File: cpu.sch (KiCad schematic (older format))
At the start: 24 parts, among them SW1 RESET, SW2 STEP, U1 Z80CPU, U2 74HC04, Y1 7.3728MHz

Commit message: New layout complete. Now with rc2014 compat. slots!
Plus on board address decoding, single stepping using M1 line so button
is click per instruction. Board is also much smaller!
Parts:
- removed C6: 1uF, Capacitors_ThroughHole:C_Radial_D5_L11_P2.5, symbol CP
- removed D2, D3: LED, LEDs:LED-3MM, symbol LED
- removed D8: D, Diodes_ThroughHole:Diode_DO-41_SOD81_Horizontal_RM10, symbol D
- removed JP1: JUMPER3, Pin_Headers:Pin_Header_Straight_1x03, symbol JUMPER3
- removed R11: 1K, Resistors_ThroughHole:Resistor_Horizontal_RM7mm, symbol R
- removed R12, R14: 220, Resistors_ThroughHole:Resistor_Horizontal_RM7mm, symbol R
- removed R13: 82K, Resistors_ThroughHole:Resistor_Horizontal_RM7mm, symbol R
- removed R15: 18K, Resistors_ThroughHole:Resistor_Horizontal_RM7mm, symbol R
- added C10, C6, C8, C9: 10n, Capacitors_ThroughHole:C_Disc_D3_P2.5, symbol C
- added JP1: JUMPER, Pin_Headers:Pin_Header_Straight_1x02, symbol JUMPER
- added R2: 1M, Resistors_ThroughHole:Resistor_Horizontal_RM7mm, symbol R
- added R3, R7: 1K, Resistors_ThroughHole:Resistor_Horizontal_RM7mm, symbol R
- added R6: 10K, Resistors_ThroughHole:Resistor_Horizontal_RM7mm, symbol R
- added U4, U6: LM555N, Housings_DIP:DIP-8_W7.62mm_LongPads, symbol LM555N
- added U5: 74HC74, Housings_DIP:DIP-14_W7.62mm_LongPads, symbol 74HC74
- C1, C12: value 100nF -> 100n
- R5: value 1M -> 1K
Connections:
- wire segments 140 -> 155
- no-connect marks 1 -> 8
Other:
- moved on the sheet: C1, C12, C2, C3, R1, RR1, SW1, U1

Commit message: Another new board layout. Few tidy ups.
Removed the single step circuit, not worth the board space and headache.
Added legend for the IO slot for easy reference. Still toying where to
put the power LED, annoying me with that resistor. Think I'm happy with
it now. Spaced things out a little to make it easy for manufacture, made
sure no traces are near board edges as much as possible.
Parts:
- removed C10, C6, C8, C9: 10n, Capacitors_ThroughHole:C_Disc_D3_P2.5, symbol C
- removed JP1: JUMPER, Pin_Headers:Pin_Header_Straight_1x02, symbol JUMPER
- removed R5, R7: 1K, Resistors_ThroughHole:Resistor_Horizontal_RM7mm, symbol R
- removed R6: 10K, Resistors_ThroughHole:Resistor_Horizontal_RM7mm, symbol R
- removed SW2: STEP, Buttons_Switches_ThroughHole:SW_PUSH_SMALL, symbol SW_PUSH
- removed unit 4 of U2
- removed unit 6 of U2
- removed U4, U6: LM555N, Housings_DIP:DIP-8_W7.62mm_LongPads, symbol LM555N
- removed U5: 74HC74, Housings_DIP:DIP-14_W7.62mm_LongPads, symbol 74HC74
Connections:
- wire segments 155 -> 116
- no-connect marks 8 -> 4

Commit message: * Replaced one card slot with an updated expansion connector. * Replaced '138 with GAL. * Implemented interrupt priority lines IEI/IEO. * Replaced discrete oscillator with 14/8 pin DIP oscillator block.
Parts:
- removed C4, C5: 22pF, Capacitors_ThroughHole:C_Disc_D3_P2.5, symbol C
- removed R2: 1M, Resistors_ThroughHole:Resistor_Horizontal_RM7mm, symbol R
- removed R3: 1K, Resistors_ThroughHole:Resistor_Horizontal_RM7mm, symbol R
- removed U2: 74HC04, Housings_DIP:DIP-14_W7.62mm_LongPads, symbol 74HC04
- removed Y1: 7.3728MHz, Crystals:Crystal_HC49-U_Vertical, symbol Crystal
- added U?: DIP_OSCILLATOR, symbol DIP_OSCILLATOR
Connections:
- wire segments 116 -> 104
- no-connect marks 4 -> 2
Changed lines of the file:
@@
 LIBS:6850
 LIBS:nrc2016
+LIBS:atf16v8cv
+LIBS:62256
 LIBS:z80-cache
 EELAYER 25 0
@@
 D7
 $Comp
-L VCC #PWR010
+L VCC #PWR16
 U 1 1 577A54FB
 P 8250 950
-F 0 "#PWR010" H 8250 800 50  0001 C CNN
+F 0 "#PWR16" H 8250 800 50  0001 C CNN
 F 1 "VCC" H 8250 1100 50  0000 C CNN
 F 2 "" H 8250 950 50  0000 C CNN
@@
 $EndComp
 $Comp
-L GND #PWR011
+L GND #PWR17
 U 1 1 577A554F
 P 8250 4250
-F 0 "#PWR011" H 8250 4000 50  0001 C CNN
+F 0 "#PWR17" H 8250 4000 50  0001 C CNN
 F 1 "GND" H 8250 4100 50  0000 C CNN
 F 2 "" H 8250 4250 50  0000 C CNN
@@
 $EndComp
 $Comp
-L GND #PWR012
+L GND #PWR11
 U 1 1 577B455D
 P 3050 1450
-F 0 "#PWR012" H 3050 1200 50  0001 C CNN
+F 0 "#PWR11" H 3050 1200 50  0001 C CNN
 F 1 "GND" H 3050 1300 50  0000 C CNN
 F 2 "" H 3050 1450 50  0000 C CNN
@@
 $EndComp
 $Comp
-L GND #PWR013
+L GND #PWR12
 U 1 1 577B48FE
 P 4050 1450
-F 0 "#PWR013" H 4050 1200 50  0001 C CNN
+F 0 "#PWR12" H 4050 1200 50  0001 C CNN
 F 1 "GND" H 4050 1300 50  0000 C CNN
 F 2 "" H 4050 1450 50  0000 C CNN
@@
 $EndComp
 $Comp
-L VCC #PWR014
+L VCC #PWR14
 U 1 1 577B4D04
 P 4650 650
-F 0 "#PWR014" H 4650 500 50  0001 C CNN
+F 0 "#PWR14" H 4650 500 50  0001 C CNN
 F 1 "VCC" H 4650 800 50  0000 C CNN
 F 2 "" H 4650 650 50  0000 C CNN
@@
 $EndComp
 $Comp
-L GND #PWR015
+L GND #PWR19
 U 1 1 577B59DE
 P 9750 6050
-F 0 "#PWR015" H 9750 5800 50  0001 C CNN
+F 0 "#PWR19" H 9750 5800 50  0001 C CNN
 F 1 "GND" H 9750 5900 50  0000 C CNN
 F 2 "" H 9750 6050 50  0000 C CNN
@@
 $EndComp
 $Comp
-L GND #PWR016
+L GND #PWR21
 U 1 1 577B5A43
 P 10150 6050
-F 0 "#PWR016" H 10150 5800 50  0001 C CNN
+F 0 "#PWR21" H 10150 5800 50  0001 C CNN
 F 1 "GND" H 10150 5900 50  0000 C CNN
 F 2 "" H 10150 6050 50  0000 C CNN
@@
 $EndComp
 $Comp
-L VCC #PWR017
+L VCC #PWR22
 U 1 1 5794221C
 P 10550 5600
-F 0 "#PWR017" H 10550 5450 50  0001 C CNN
+F 0 "#PWR22" H 10550 5450 50  0001 C CNN
 F 1 "VCC" H 10550 5750 50  0000 C CNN
 F 2 "" H 10550 5600 50  0000 C CNN
@@
 $EndComp
 $Comp
-L GND #PWR018
+L GND #PWR23
 U 1 1 57942290
 P 10550 6100
-F 0 "#PWR018" H 10550 5850 50  0001 C CNN
+F 0 "#PWR23" H 10550 5850 50  0001 C CNN
 F 1 "GND" H 10550 5950 50  0000 C CNN
 F 2 "" H 10550 6100 50  0000 C CNN
@@
 $EndComp
 $Comp
-L VCC #PWR019
+L VCC #PWR15
 U 1 1 57945470
 P 6100 1550
-F 0 "#PWR019" H 6100 1400 50  0001 C CNN
+F 0 "#PWR15" H 6100 1400 50  0001 C CNN
 F 1 "VCC" H 6100 1700 50  0000 C CNN
 F 2 "" H 6100 1550 50  0000 C CNN
@@
 	1    0    0    -1
 $EndComp
-$Comp
-L R R2
-U 1 1 57991B52
-P 1350 1650
-F 0 "R2" V 1430 1650 50  0000 C CNN
-F 1 "1M" V 1350 1650 50  0000 C CNN
-F 2 "Resistors_ThroughHole:Resistor_Horizontal_RM7mm" V 1280 1650 50  0001 C CNN
-F 3 "" H 1350 1650 50  0000 C CNN
-	1    1350 1650
-	0    1    1    0
-$EndComp
-$Comp
-L R R3
-U 1 1 57991D5E
-P 1850 2300
-F 0 "R3" V 1930 2300 50  0000 C CNN
-F 1 "1K" V 1850 2300 50  0000 C CNN
-F 2 "Resistors_ThroughHole:Resistor_Horizontal_RM7mm" V 1780 2300 50  0001 C CNN
-F 3 "" H 1850 2300 50  0000 C CNN
-	1    1850 2300
-	1    0    0    -1
-$EndComp
-$Comp
-L Crystal Y1
-U 1 1 57991DBB
-P 1350 2550
-F 0 "Y1" H 1350 2700 50  0000 C CNN
-F 1 "7.3728MHz" H 1350 2400 50  0000 C CNN
-F 2 "Crystals:Crystal_HC49-U_Vertical" H 1350 2550 50  0001 C CNN
-F 3 "" H 1350 2550 50  0000 C CNN
-	1    1350 2550
-	1    0    0    -1
-$EndComp
-$Comp
-L C C4
-U 1 1 579921C3
-P 850 2800
-F 0 "C4" H 875 2900 50  0000 L CNN
-F 1 "22pF" H 875 2700 50  0000 L CNN
-F 2 "Capacitors_ThroughHole:C_Disc_D3_P2.5" H 888 2650 50  0001 C CNN
-F 3 "" H 850 2800 50  0000 C CNN
-	1    850  2800
-	1    0    0    -1
-$EndComp
-$Comp
-L C C5
-U 1 1 57992226
-P 1850 2800
-F 0 "C5" H 1875 2900 50  0000 L CNN
-F 1 "22pF" H 1875 2700 50  0000 L CNN
-F 2 "Capacitors_ThroughHole:C_Disc_D3_P2.5" H 1888 2650 50  0001 C CNN
-F 3 "" H 1850 2800 50  0000 C CNN
-	1    1850 2800
-	1    0    0    -1
-$EndComp
-$Comp
-L GND #PWR020
-U 1 1 579925A6
-P 850 3050
-F 0 "#PWR020" H 850 2800 50  0001 C CNN
-F 1 "GND" H 850 2900 50  0000 C CNN
-F 2 "" H 850 3050 50  0000 C CNN
-F 3 "" H 850 3050 50  0000 C CNN
-	1    850  3050
-	1    0    0    -1
-$EndComp
-$Comp
-L GND #PWR021
-U 1 1 579925F6
-P 1850 3050
-F 0 "#PWR021" H 1850 2800 50  0001 C CNN
-F 1 "GND" H 1850 2900 50  0000 C CNN
-F 2 "" H 1850 3050 50  0000 C CNN
-F 3 "" H 1850 3050 50  0000 C CNN
-	1    1850 3050
-	1    0    0    -1
-$EndComp
 Text Label 7250 2200 0    60   ~ 0
 ~M1
@@
 ~WAIT
 $Comp
-L 74HC04 U2
-U 1 1 57997E58
-P 1350 2050
-F 0 "U2" H 1500 2150 50  0000 C CNN
-F 1 "74HC04" H 1550 1950 50  0000 C CNN
-F 2 "Housings_DIP:DIP-14_W7.62mm_LongPads" H 1350 2050 50  0001 C CNN
-F 3 "" H 1350 2050 50  0000 C CNN
-	1    1350 2050
-	1    0    0    -1
-$EndComp
-$Comp
-L 74HC04 U2
-U 2 1 579987FC
-P 2350 2050
-F 0 "U2" H 2500 2150 50  0000 C CNN
-F 1 "74HC04" H 2550 1950 50  0000 C CNN
-F 2 "Housings_DIP:DIP-14_W7.62mm_LongPads" H 2350 2050 50  0001 C CNN
-F 3 "" H 2350 2050 50  0000 C CNN
-	2    2350 2050
-	1    0    0    -1
-$EndComp
-$Comp
-L VCC #PWR022
+L VCC #PWR20
 U 1 1 579C0903
 P 10150 5600
-F 0 "#PWR022" H 10150 5450 50  0001 C CNN
+F 0 "#PWR20" H 10150 5450 50  0001 C CNN
 F 1 "VCC" H 10150 5750 50  0000 C CNN
 F 2 "" H 10150 5600 50  0000 C CNN
@@
 $EndComp
 $Comp
-L VCC #PWR023
+L VCC #PWR18
 U 1 1 579C0968
 P 9750 5600
-F 0 "#PWR023" H 9750 5450 50  0001 C CNN
+F 0 "#PWR18" H 9750 5450 50  0001 C CNN
 F 1 "VCC" H 9750 5750 50  0000 C CNN
 F 2 "" H 9750 5600 50  0000 C CNN
@@
 Connection ~ 7200 3400
 Wire Wire Line
-	1850 1650 1850 2150
-Wire Wire Line
-	850  1650 850  2650
-Wire Wire Line
-	1200 1650 850  1650
-Wire Wire Line
-	1500 1650 1850 1650
-Wire Wire Line
-	1500 2550 1850 2550
-Wire Wire Line
-	1850 2450 1850 2650
-Wire Wire Line
-	850  2550 1200 2550
-Connection ~ 1850 2550
-Connection ~ 850  2550
-Wire Wire Line
-	850  2950 850  3050
-Wire Wire Line
-	1850 2950 1850 3050
-Wire Wire Line
 	4050 700  4200 700
 Wire Wire Line
@@
 Connection ~ 5800 1750
 Wire Wire Line
-	900  2050 850  2050
-Connection ~ 850  2050
-Wire Wire Line
-	1800 2050 1900 2050
-Connection ~ 1850 2050
-Wire Wire Line
 	7100 1750 7100 3100
 Connection ~ 7100 3100
@@
 Connection ~ 7000 2000
 $Comp
-L 74HC04 U2
-U 3 1 579DE204
-P 4750 2950
-F 0 "U2" H 4900 3050 50  0000 C CNN
-F 1 "74HC04" H 4950 2850 50  0000 C CNN
-F 2 "Housings_DIP:DIP-14_W7.62mm_LongPads" H 4750 2950 50  0001 C CNN
-F 3 "" H 4750 2950 50  0000 C CNN
-	3    4750 2950
-	1    0    0    -1
-$EndComp
-$Comp
-L 74HC04 U2
-U 5 1 579DE2CC
-P 4750 3350
-F 0 "U2" H 4900 3450 50  0000 C CNN
-F 1 "74HC04" H 4950 3250 50  0000 C CNN
-F 2 "Housings_DIP:DIP-14_W7.62mm_LongPads" H 4750 3350 50  0001 C CNN
-F 3 "" H 4750 3350 50  0000 C CNN
-	5    4750 3350
-	1    0    0    -1
-$EndComp
-Wire Wire Line
-	4300 2950 4200 2950
-Wire Wire Line
-	4200 2750 4200 3350
-Wire Wire Line
-	4200 3350 4300 3350
-Connection ~ 4200 2950
-$Comp
-L VCC #PWR024
+L VCC #PWR13
 U 1 1 579DE54D
-P 4200 2750
-F 0 "#PWR024" H 4200 2600 50  0001 C CNN
-F 1 "VCC" H 4200 2900 50  0000 C CNN
-F 2 "" H 4200 2750 50  0000 C CNN
-F 3 "" H 4200 2750 50  0000 C CNN
-	1    4200 2750
-	1    0    0    -1
-$EndComp
-NoConn ~ 5200 2950
-NoConn ~ 5200 3350
+P 2500 1450
+F 0 "#PWR13" H 2500 1300 50  0001 C CNN
+F 1 "VCC" H 2500 1600 50  0000 C CNN
+F 2 "" H 2500 1450 50  0000 C CNN
+F 3 "" H 2500 1450 50  0000 C CNN
+	1    2500 1450
+	1    0    0    -1
+$EndComp
 NoConn ~ 6100 2500
+$Comp
+L DIP_OSCILLATOR U?
+U 1 1 57C09843
+P 2300 2350
+F 0 "U?" H 2650 2300 60  0000 C CNN
+F 1 "DIP_OSCILLATOR" V 2250 2650 60  0000 C CNN
+F 2 "" H 2300 2350 60  0000 C CNN
+F 3 "" H 2300 2350 60  0000 C CNN
+	1    2300 2350
+	1    0    0    -1
+$EndComp
+Wire Wire Line
+	2500 1450 2500 1650
+$Comp
+L GND #PWR?
+U 1 1 57C09D2A
+P 2500 2600
+F 0 "#PWR?" H 2500 2350 50  0001 C CNN
+F 1 "GND" H 2500 2450 50  0000 C CNN
+F 2 "" H 2500 2600 50  0000 C CNN
+F 3 "" H 2500 2600 50  0000 C CNN
+	1    2500 2600
+	1    0    0    -1
+$EndComp
+Wire Wire Line
+	2500 2600 2500 2450
 $EndSCHEMATC

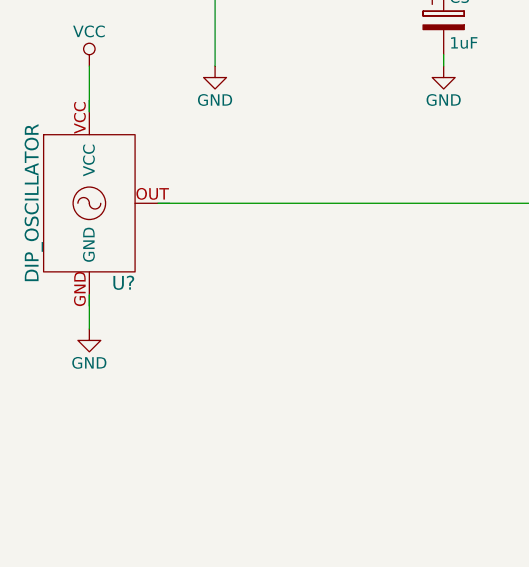
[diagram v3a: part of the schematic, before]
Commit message: Fixed schema DRC errors
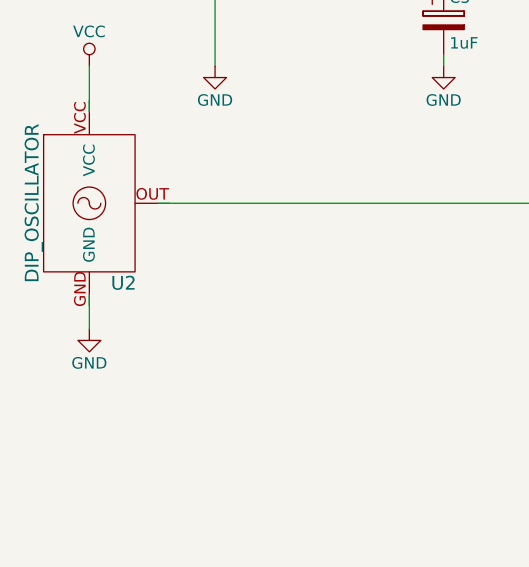
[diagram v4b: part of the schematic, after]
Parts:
- gave numbers to parts that had none: 1
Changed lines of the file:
@@
 D7
 $Comp
-L VCC #PWR16
+L VCC #PWR06
 U 1 1 577A54FB
 P 8250 950
-F 0 "#PWR16" H 8250 800 50  0001 C CNN
+F 0 "#PWR06" H 8250 800 50  0001 C CNN
 F 1 "VCC" H 8250 1100 50  0000 C CNN
 F 2 "" H 8250 950 50  0000 C CNN
@@
 $EndComp
 $Comp
-L GND #PWR17
+L GND #PWR07
 U 1 1 577A554F
 P 8250 4250
-F 0 "#PWR17" H 8250 4000 50  0001 C CNN
+F 0 "#PWR07" H 8250 4000 50  0001 C CNN
 F 1 "GND" H 8250 4100 50  0000 C CNN
 F 2 "" H 8250 4250 50  0000 C CNN
@@
 $EndComp
 $Comp
-L GND #PWR11
+L GND #PWR08
 U 1 1 577B455D
 P 3050 1450
-F 0 "#PWR11" H 3050 1200 50  0001 C CNN
+F 0 "#PWR08" H 3050 1200 50  0001 C CNN
 F 1 "GND" H 3050 1300 50  0000 C CNN
 F 2 "" H 3050 1450 50  0000 C CNN
@@
 $EndComp
 $Comp
-L GND #PWR12
+L GND #PWR09
 U 1 1 577B48FE
 P 4050 1450
-F 0 "#PWR12" H 4050 1200 50  0001 C CNN
+F 0 "#PWR09" H 4050 1200 50  0001 C CNN
 F 1 "GND" H 4050 1300 50  0000 C CNN
 F 2 "" H 4050 1450 50  0000 C CNN
@@
 $EndComp
 $Comp
-L VCC #PWR14
+L VCC #PWR010
 U 1 1 577B4D04
 P 4650 650
-F 0 "#PWR14" H 4650 500 50  0001 C CNN
+F 0 "#PWR010" H 4650 500 50  0001 C CNN
 F 1 "VCC" H 4650 800 50  0000 C CNN
 F 2 "" H 4650 650 50  0000 C CNN
@@
 $EndComp
 $Comp
-L GND #PWR19
+L GND #PWR011
 U 1 1 577B59DE
 P 9750 6050
-F 0 "#PWR19" H 9750 5800 50  0001 C CNN
+F 0 "#PWR011" H 9750 5800 50  0001 C CNN
 F 1 "GND" H 9750 5900 50  0000 C CNN
 F 2 "" H 9750 6050 50  0000 C CNN
@@
 $EndComp
 $Comp
-L GND #PWR21
+L GND #PWR012
 U 1 1 577B5A43
 P 10150 6050
-F 0 "#PWR21" H 10150 5800 50  0001 C CNN
+F 0 "#PWR012" H 10150 5800 50  0001 C CNN
 F 1 "GND" H 10150 5900 50  0000 C CNN
 F 2 "" H 10150 6050 50  0000 C CNN
@@
 $EndComp
 $Comp
-L VCC #PWR22
+L VCC #PWR013
 U 1 1 5794221C
 P 10550 5600
-F 0 "#PWR22" H 10550 5450 50  0001 C CNN
+F 0 "#PWR013" H 10550 5450 50  0001 C CNN
 F 1 "VCC" H 10550 5750 50  0000 C CNN
 F 2 "" H 10550 5600 50  0000 C CNN
@@
 $EndComp
 $Comp
-L GND #PWR23
+L GND #PWR014
 U 1 1 57942290
 P 10550 6100
-F 0 "#PWR23" H 10550 5850 50  0001 C CNN
+F 0 "#PWR014" H 10550 5850 50  0001 C CNN
 F 1 "GND" H 10550 5950 50  0000 C CNN
 F 2 "" H 10550 6100 50  0000 C CNN
@@
 $EndComp
 $Comp
-L VCC #PWR15
+L VCC #PWR015
 U 1 1 57945470
 P 6100 1550
-F 0 "#PWR15" H 6100 1400 50  0001 C CNN
+F 0 "#PWR015" H 6100 1400 50  0001 C CNN
 F 1 "VCC" H 6100 1700 50  0000 C CNN
 F 2 "" H 6100 1550 50  0000 C CNN
@@
 ~WAIT
 $Comp
-L VCC #PWR20
+L VCC #PWR016
 U 1 1 579C0903
 P 10150 5600
-F 0 "#PWR20" H 10150 5450 50  0001 C CNN
+F 0 "#PWR016" H 10150 5450 50  0001 C CNN
 F 1 "VCC" H 10150 5750 50  0000 C CNN
 F 2 "" H 10150 5600 50  0000 C CNN
@@
 $EndComp
 $Comp
-L VCC #PWR18
+L VCC #PWR017
 U 1 1 579C0968
 P 9750 5600
-F 0 "#PWR18" H 9750 5450 50  0001 C CNN
+F 0 "#PWR017" H 9750 5450 50  0001 C CNN
 F 1 "VCC" H 9750 5750 50  0000 C CNN
 F 2 "" H 9750 5600 50  0000 C CNN
@@
 Connection ~ 7000 2000
 $Comp
-L VCC #PWR13
+L VCC #PWR018
 U 1 1 579DE54D
 P 2500 1450
-F 0 "#PWR13" H 2500 1300 50  0001 C CNN
+F 0 "#PWR018" H 2500 1300 50  0001 C CNN
 F 1 "VCC" H 2500 1600 50  0000 C CNN
 F 2 "" H 2500 1450 50  0000 C CNN
@@
 NoConn ~ 6100 2500
 $Comp
-L DIP_OSCILLATOR U?
+L DIP_OSCILLATOR U2
 U 1 1 57C09843
 P 2300 2350
-F 0 "U?" H 2650 2300 60  0000 C CNN
+F 0 "U2" H 2650 2300 60  0000 C CNN
 F 1 "DIP_OSCILLATOR" V 2250 2650 60  0000 C CNN
 F 2 "" H 2300 2350 60  0000 C CNN
@@
 	2500 1450 2500 1650
 $Comp
-L GND #PWR?
+L GND #PWR019
 U 1 1 57C09D2A
 P 2500 2600
-F 0 "#PWR?" H 2500 2350 50  0001 C CNN
+F 0 "#PWR019" H 2500 2350 50  0001 C CNN
 F 1 "GND" H 2500 2450 50  0000 C CNN
 F 2 "" H 2500 2600 50  0000 C CNN

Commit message: Added new expansion and GAL to layout.
Haven't routed the osc. or the reset.
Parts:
- U2: footprint (none) -> Oscillators:OSC_DIP8
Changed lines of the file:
@@
 F 0 "U2" H 2650 2300 60  0000 C CNN
 F 1 "DIP_OSCILLATOR" V 2250 2650 60  0000 C CNN
-F 2 "" H 2300 2350 60  0000 C CNN
+F 2 "Oscillators:OSC_DIP8" H 2300 2350 60  0001 C CNN
 F 3 "" H 2300 2350 60  0000 C CNN
 	1    2300 2350

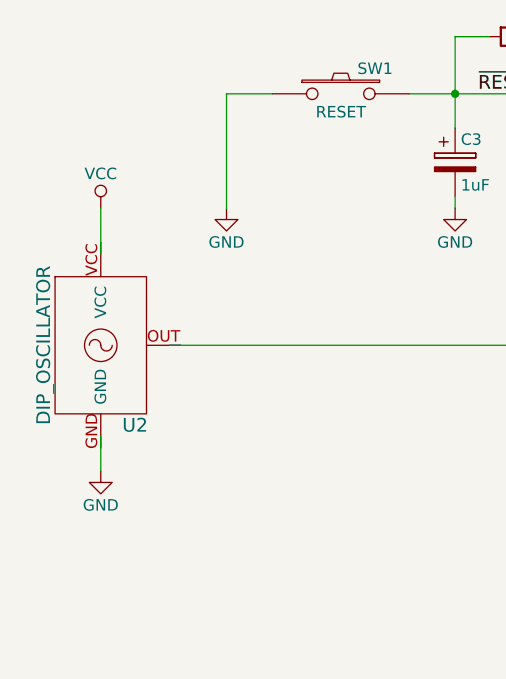
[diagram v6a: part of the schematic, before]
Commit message: * fixed DRC errors on pin 1 of Px2 connectors. * fixed unconnected ground pin issue of GAL. * added 8DIP and 14DIP oscillator block footprint. * updated bottom silkscreen. * added via stitching in a few places for better GND net. * routed the reset and oscillator circuits. * Design passes KiCAD DRC.
!! This is NRC016 RC1 !!
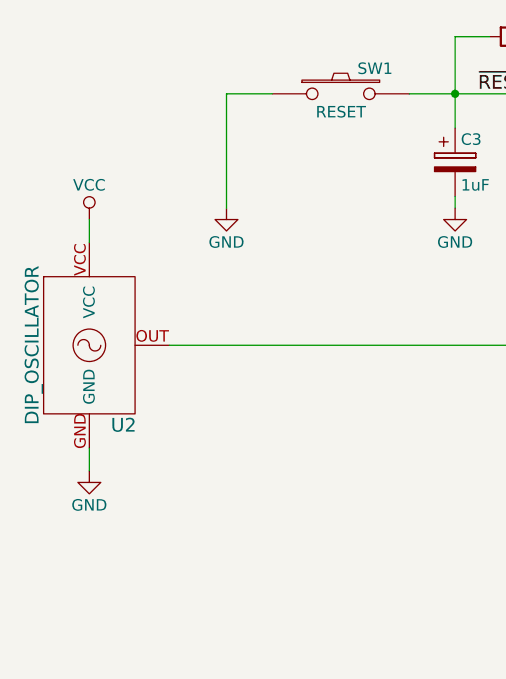
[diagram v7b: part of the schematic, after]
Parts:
- U2: footprint Oscillators:OSC_DIP8 -> nrc2016:OSC_MULTIPACKAGE_DIP
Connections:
- net GND: now also U2.GND
- net VCC: now also U2.VCC
- net ~CLK: now also U2.OUT
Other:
- moved on the sheet: U2
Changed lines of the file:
@@
 L VCC #PWR018
 U 1 1 579DE54D
-P 2500 1450
-F 0 "#PWR018" H 2500 1300 50  0001 C CNN
-F 1 "VCC" H 2500 1600 50  0000 C CNN
-F 2 "" H 2500 1450 50  0000 C CNN
-F 3 "" H 2500 1450 50  0000 C CNN
-	1    2500 1450
+P 2450 1500
+F 0 "#PWR018" H 2450 1350 50  0001 C CNN
+F 1 "VCC" H 2450 1650 50  0000 C CNN
+F 2 "" H 2450 1500 50  0000 C CNN
+F 3 "" H 2450 1500 50  0000 C CNN
+	1    2450 1500
 	1    0    0    -1
 $EndComp
@@
 L DIP_OSCILLATOR U2
 U 1 1 57C09843
-P 2300 2350
-F 0 "U2" H 2650 2300 60  0000 C CNN
-F 1 "DIP_OSCILLATOR" V 2250 2650 60  0000 C CNN
-F 2 "Oscillators:OSC_DIP8" H 2300 2350 60  0001 C CNN
-F 3 "" H 2300 2350 60  0000 C CNN
-	1    2300 2350
+P 2250 2350
+F 0 "U2" H 2600 2300 60  0000 C CNN
+F 1 "DIP_OSCILLATOR" V 2200 2650 60  0000 C CNN
+F 2 "nrc2016:OSC_MULTIPACKAGE_DIP" H 2250 2350 60  0001 C CNN
+F 3 "" H 2250 2350 60  0000 C CNN
+	1    2250 2350
+	1    0    0    -1
+$EndComp
+$Comp
+L GND #PWR019
+U 1 1 57C09D2A
+P 2450 2600
+F 0 "#PWR019" H 2450 2350 50  0001 C CNN
+F 1 "GND" H 2450 2450 50  0000 C CNN
+F 2 "" H 2450 2600 50  0000 C CNN
+F 3 "" H 2450 2600 50  0000 C CNN
+	1    2450 2600
 	1    0    0    -1
 $EndComp
 Wire Wire Line
-	2500 1450 2500 1650
-$Comp
-L GND #PWR019
-U 1 1 57C09D2A
-P 2500 2600
-F 0 "#PWR019" H 2500 2350 50  0001 C CNN
-F 1 "GND" H 2500 2450 50  0000 C CNN
-F 2 "" H 2500 2600 50  0000 C CNN
-F 3 "" H 2500 2600 50  0000 C CNN
-	1    2500 2600
-	1    0    0    -1
-$EndComp
+	2450 2600 2450 2500
 Wire Wire Line
-	2500 2600 2500 2450
+	2450 1600 2450 1500
 $EndSCHEMATC
